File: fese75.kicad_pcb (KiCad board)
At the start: 2 copper layers, 319.1 x 133.3 mm, 209 parts, among them J1 MX-NoLED, J2 USB_C_Receptacle_USB2.0, K1 MX-NoLED, M1 MX-NoLED, P1 MX-NoLED, Q1 MX-NoLED, SW1 RotaryEncoder_Switch, T1 MX-NoLED, U1 MX-NoLED, U2 ATmega32U4-A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

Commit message: Finalize1
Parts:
- removed REF** (x3): Stabilizer_Cherry_MX_2u, Mounting_Keyboard_Stabilizer:Stabilizer_Cherry_MX_2u
- removed REF**: Stabilizer_Cherry_MX_6.25u, Mounting_Keyboard_Stabilizer:Stabilizer_Cherry_MX_6.25u
- TP1: footprint TestPoint:TestPoint_THTPad_2.0x2.0mm_Drill1.0mm -> TestPoint:TestPoint_THTPad_D1.0mm_Drill0.5mm
- TP10: value TestPoint -> CO8; moved to B.Cu
- TP11: value TestPoint -> CO9; moved to B.Cu
- TP12: value TestPoint -> CO10; moved to B.Cu
- TP13: value TestPoint -> CO11; moved to B.Cu
- TP14: value TestPoint -> CO12; moved to B.Cu
- TP15: value TestPoint -> CO13; moved to B.Cu
- TP16: value TestPoint -> CO14; moved to B.Cu
- TP17: value TestPoint -> CO15; moved to B.Cu
- TP18: value TestPoint -> RO1; moved to B.Cu
- TP19: value TestPoint -> RO2; moved to B.Cu
- TP2: footprint TestPoint:TestPoint_THTPad_D2.0mm_Drill1.0mm -> TestPoint:TestPoint_THTPad_1.0x1.0mm_Drill0.5mm
- TP20: value TestPoint -> RO3; moved to B.Cu
- TP21: value TestPoint -> RO4; moved to B.Cu
- TP22: value TestPoint -> RO5; moved to B.Cu
- TP23: value TestPoint -> RO6; moved to B.Cu
- TP3, TP4, TP5, TP6: moved to B.Cu
- TP7: value TestPoint -> CO5; moved to B.Cu
- TP8: value TestPoint -> CO6; moved to B.Cu
- TP9: value TestPoint -> CO7; moved to B.Cu
- turned TP10 to 180 degrees
- turned TP11 to 180 degrees
- turned TP12 to 180 degrees
- turned TP13 to 180 degrees
- turned TP14 to 180 degrees
- turned TP15 to 180 degrees
- turned TP16 to 180 degrees
- turned TP17 to 180 degrees
- turned TP18 to 180 degrees
- turned TP19 to 0 degrees
- turned TP20 to 0 degrees
- turned TP21 to 0 degrees
- turned TP22 to 0 degrees
- turned TP23 to 0 degrees
- turned TP3 to 180 degrees
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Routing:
- net COL3: track 316.0 -> 328.7 mm, vias 7 -> 8

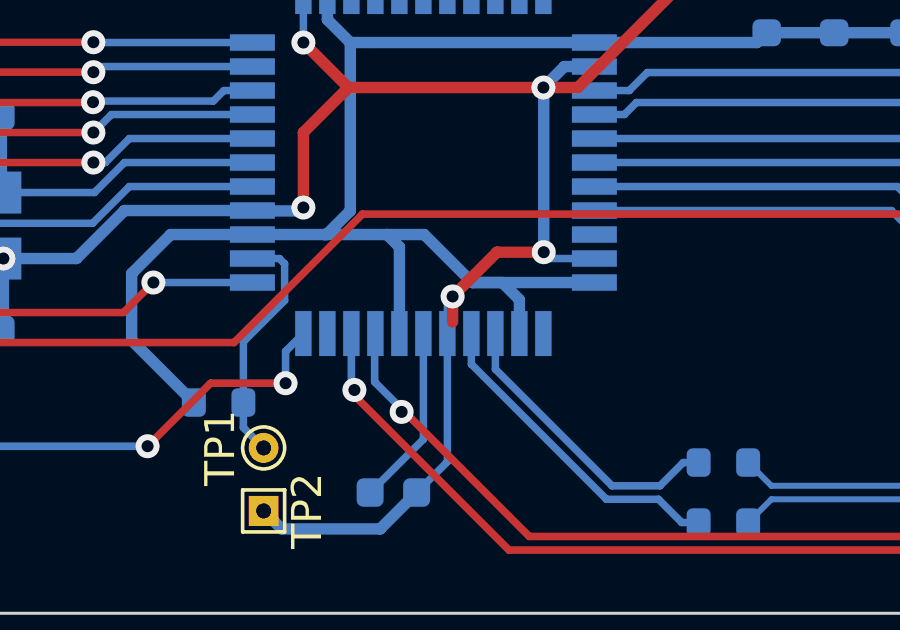
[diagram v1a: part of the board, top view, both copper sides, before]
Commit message: connect missing trace
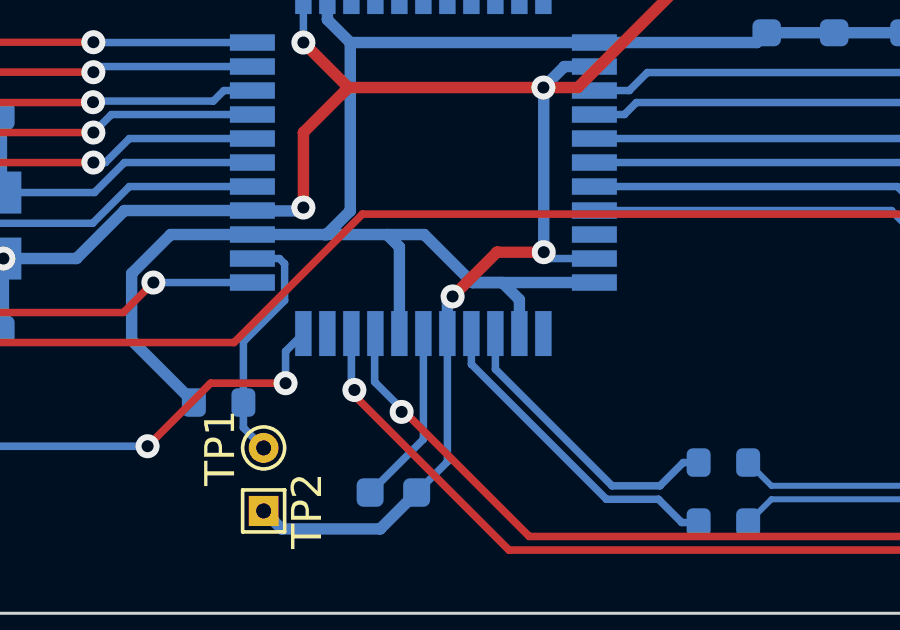
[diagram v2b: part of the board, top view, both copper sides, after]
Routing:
- net GND: track 326.8 -> 326.0 mm
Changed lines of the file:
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@@
   (segment (start 337.75 67.327222) (end 337.75 67.8875) (width 0.381) (layer "F.Cu") (net 108))
   (segment (start 331.336229 57.099979) (end 327.79375 53.5575) (width 0.381) (layer "F.Cu") (net 108))
-  (segment (start 200.898998 172.101002) (end 200.898998 171.251497) (width 0.381) (layer "F.Cu") (net 108))
   (segment (start 202.375294 169.775201) (end 203.937299 169.775201) (width 0.381) (layer "F.Cu") (net 108))
   (segment (start 184.225006 168.287497) (end 185.925003 169.987493) (width 0.381) (layer "F.Cu") (net 108))
@@
   (segment (start 198.4875 179) (end 195.2 179) (width 0.381) (layer "B.Cu") (net 108))
   (segment (start 327.42375 53.1875) (end 327.79375 53.5575) (width 0.381) (layer "B.Cu") (net 108))
-  (segment (start 200.725 171.425495) (end 200.898998 171.251497) (width 0.25) (layer "B.Cu") (net 108))
   (segment (start 188.36071 169.987493) (end 185.925003 169.987493) (width 0.381) (layer "B.Cu") (net 108))
   (segment (start 203.937299 164.299799) (end 203.937299 169.775201) (width 0.381) (layer "B.Cu") (net 108))
+  (segment (start 200.725 171.425495) (end 200.898998 171.251497) (width 0.381) (layer "B.Cu") (net 108))
   (segment (start 189.960718 168.3875) (end 188.360718 169.9875) (width 0.381) (layer "B.Cu") (net 108))
   (segment (start 319.14375 50.1775) (end 327.79375 50.1775) (width 0.381) (layer "B.Cu") (net 108))
@@
   (segment (start 185.925 172.29375) (end 185.85 172.36875) (width 0.25) (layer "B.Cu") (net 108))
   (segment (start 203.937299 169.775201) (end 204.149598 169.9875) (width 0.25) (layer "B.Cu") (net 108))
+  (segment (start 200.725 172.4875) (end 200.725 171.425495) (width 0.381) (layer "B.Cu") (net 108))
   (segment (start 210.24375 159.7875) (end 211.36875 160.9125) (width 0.381) (layer "B.Cu") (net 108))
   (segment (start 200.725 176.7625) (end 200.725 172.4875) (width 0.25) (layer "B.Cu") (net 108))
@@
   (segment (start 195.2 179) (end 194.6 178.4) (width 0.381) (layer "B.Cu") (net 108))
   (segment (start 199.7 177.7875) (end 200.725 176.7625) (width 0.25) (layer "B.Cu") (net 108))
-  (segment (start 200.725 172.4875) (end 200.725 171.425495) (width 0.25) (layer "B.Cu") (net 108))
   (segment (start 198.15 177.7875) (end 199.925 176.0125) (width 0.25) (layer "B.Cu") (net 109))
   (segment (start 199.925 176.0125) (end 199.925 172.4875) (width 0.25) (layer "B.Cu") (net 109))

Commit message: fix missing stab bug
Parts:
- added REF**: Stabilizer_Cherry_MX_2u, Mounting_Keyboard_Stabilizer:Stabilizer_Cherry_MX_2u, F.Cu at (299.6, 88.9)
- added REF**: Stabilizer_Cherry_MX_2u, Mounting_Keyboard_Stabilizer:Stabilizer_Cherry_MX_2u, F.Cu at (54.4, 146.1)
- added REF**: Stabilizer_Cherry_MX_2u, Mounting_Keyboard_Stabilizer:Stabilizer_Cherry_MX_2u, F.Cu at (297.2, 127.0)
- added REF**: Stabilizer_Cherry_MX_6.25u, Mounting_Keyboard_Stabilizer:Stabilizer_Cherry_MX_6.25u, F.Cu at (163.9, 165.1)
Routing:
- net ROW5: track 314.6 -> 316.6 mm
- net ROW2: track 451.2 -> 452.4 mm
- net COL1: track 406.9 -> 407.9 mm

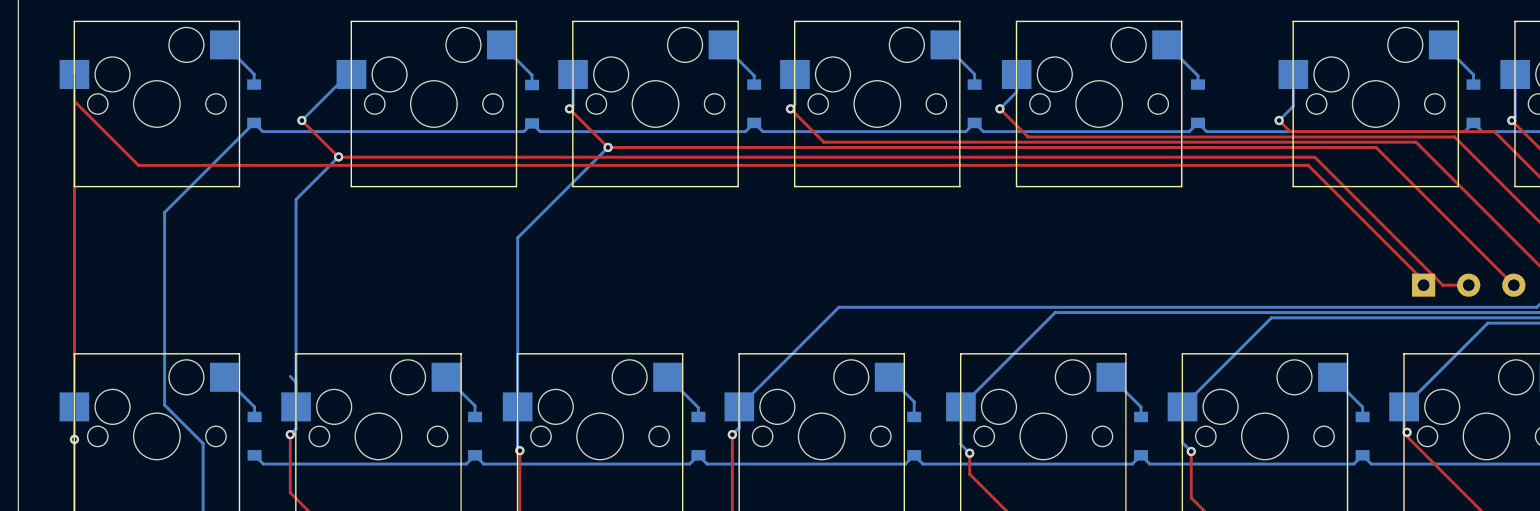
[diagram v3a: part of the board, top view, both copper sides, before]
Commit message: fix missing trace
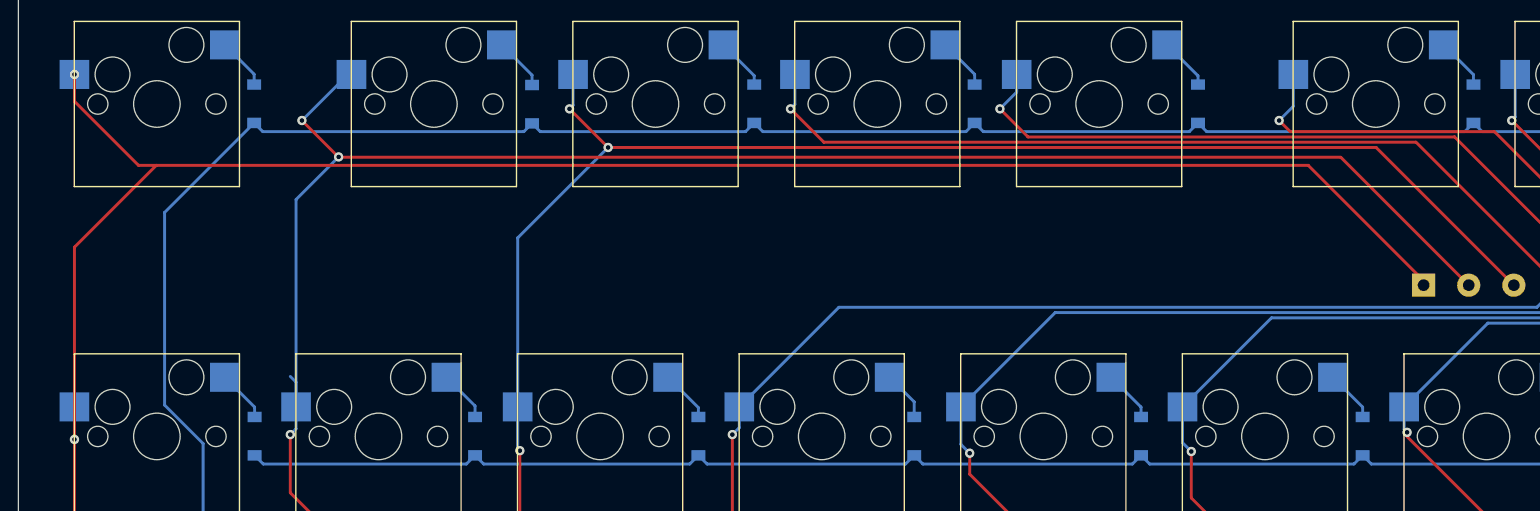
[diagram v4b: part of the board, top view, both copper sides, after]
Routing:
- net COL1: track 407.9 -> 403.2 mm, vias 6 -> 7
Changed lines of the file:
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@@
     )
     (pad_to_mask_clearance 0)
-    (grid_origin 32.93125 50.84375)
     (pcbplotparams
       (layerselection 0x00010fc_ffffffff)
@@
       (outputformat 1)
       (mirror false)
-      (drillshape 1)
+      (drillshape 0)
       (scaleselection 1)
-      (outputdirectory "")
+      (outputdirectory "C:/Users/imovi/Desktop/FESE75/Gerber/")
     )
   )
@@
   (segment (start 84.31875 124.64675) (end 84.31875 125.37125) (width 0.25) (layer "B.Cu") (net 13))
   (segment (start 76.925 146.7875) (end 70.925 152.7875) (width 0.25) (layer "F.Cu") (net 14))
-  (segment (start 58.08125 64.94375) (end 141.998562 64.94375) (width 0.254) (layer "F.Cu") (net 14))
   (segment (start 100.925 152.7875) (end 101.815625 153.678125) (width 0.25) (layer "F.Cu") (net 14))
+  (segment (start 58.08125 64.94375) (end 144.224111 64.94375) (width 0.254) (layer "F.Cu") (net 14))
   (segment (start 170.925 170.7875) (end 174.925 166.7875) (width 0.25) (layer "F.Cu") (net 14))
   (segment (start 70.925 152.7875) (end 100.925 152.7875) (width 0.25) (layer "F.Cu") (net 14))
-  (segment (start 54.925 61.7875) (end 58.08125 64.94375) (width 0.254) (layer "F.Cu") (net 14))
   (segment (start 62.925 108.7875) (end 62.925 116.7875) (width 0.25) (layer "F.Cu") (net 14))
   (segment (start 67.925 127.7875) (end 67.925 131.7875) (width 0.25) (layer "F.Cu") (net 14))
@@
   (segment (start 53.925 93.7875) (end 62.925 102.7875) (width 0.25) (layer "F.Cu") (net 14))
   (segment (start 101.815625 153.678125) (end 125.009375 153.678125) (width 0.25) (layer "F.Cu") (net 14))
-  (segment (start 152.998562 75.94375) (end 155.224111 75.94375) (width 0.254) (layer "F.Cu") (net 14))
-  (segment (start 141.998562 64.94375) (end 152.998562 75.94375) (width 0.254) (layer "F.Cu") (net 14))
+  (segment (start 54.925 61.7875) (end 58.08125 64.94375) (width 0.254) (layer "F.Cu") (net 14))
   (segment (start 67.925 131.7875) (end 76.925 140.7875) (width 0.25) (layer "F.Cu") (net 14))
   (segment (start 125.009375 153.678125) (end 142.11875 170.7875) (width 0.25) (layer "F.Cu") (net 14))
+  (segment (start 144.224111 64.94375) (end 155.224111 75.94375) (width 0.254) (layer "F.Cu") (net 14))
   (segment (start 142.11875 170.7875) (end 170.925 170.7875) (width 0.25) (layer "F.Cu") (net 14))
   (via (at 67.925 121.7875) (size 0.8) (drill 0.4) (layers "F.Cu" "B.Cu") (net 14))
@@
   (segment (start 276.89825 161.63575) (end 279.25625 163.99375) (width 0.25) (layer "B.Cu") (net 26))
   (segment (start 276.89825 160.06375) (end 276.89825 161.63575) (width 0.25) (layer "B.Cu") (net 26))
+  (segment (start 35.37125 89.20375) (end 35.37125 72.67875) (width 0.254) (layer "F.Cu") (net 27))
   (segment (start 40.13375 122.1225) (end 40.13375 139.54625) (width 0.254) (layer "F.Cu") (net 27))
+  (segment (start 35.37125 72.67875) (end 42.40625 65.64375) (width 0.254) (layer "F.Cu") (net 27))
   (segment (start 60.775 151.7875) (end 63.966771 154.979271) (width 0.254) (layer "F.Cu") (net 27))
+  (segment (start 42.40625 65.64375) (end 141.43125 65.64375) (width 0.254) (layer "F.Cu") (net 27))
   (segment (start 40.13375 105.64125) (end 40.13375 107.54625) (width 0.25) (layer "F.Cu") (net 27))
   (segment (start 69.695729 154.979271) (end 70.8875 153.7875) (width 0.254) (layer "F.Cu") (net 27))
@@
   (segment (start 43.88125 143.29375) (end 48.925 148.3375) (width 0.254) (layer "F.Cu") (net 27))
   (segment (start 38.23125 160.34375) (end 39.781783 160.34375) (width 0.254) (layer "F.Cu") (net 27))
-  (segment (start 35.37125 57.82875) (end 35.37125 58.08375) (width 0.25) (layer "F.Cu") (net 27))
   (segment (start 35.37125 89.20375) (end 35.37125 100.69125) (width 0.25) (layer "F.Cu") (net 27))
   (segment (start 40.13375 139.54625) (end 43.88125 143.29375) (width 0.254) (layer "F.Cu") (net 27))
@@
   (segment (start 48.925 151.200533) (end 48.925 150.7875) (width 0.254) (layer "F.Cu") (net 27))
   (segment (start 106.565625 160.428125) (end 120.565625 160.428125) (width 0.25) (layer "F.Cu") (net 27))
-  (segment (start 35.37125 58.08375) (end 35.37125 60.133669) (width 0.254) (layer "F.Cu") (net 27))
+  (segment (start 40.881331 65.64375) (end 42.40625 65.64375) (width 0.254) (layer "F.Cu") (net 27))
   (segment (start 49.925 151.7875) (end 60.775 151.7875) (width 0.25) (layer "F.Cu") (net 27))
   (segment (start 35.37125 100.69125) (end 40.13375 105.45375) (width 0.254) (layer "F.Cu") (net 27))
   (segment (start 141.43125 65.64375) (end 151.34554 75.55804) (width 0.254) (layer "F.Cu") (net 27))
   (segment (start 131.925 171.7875) (end 189.925 171.7875) (width 0.25) (layer "F.Cu") (net 27))
-  (segment (start 40.881331 65.64375) (end 141.43125 65.64375) (width 0.254) (layer "F.Cu") (net 27))
+  (segment (start 35.37125 60.133669) (end 35.37125 57.82875) (width 0.254) (layer "F.Cu") (net 27))
   (segment (start 39.781783 160.34375) (end 48.925 151.200533) (width 0.254) (layer "F.Cu") (net 27))
-  (segment (start 35.37125 58.08375) (end 35.37125 86.40375) (width 0.25) (layer "F.Cu") (net 27))
-  (segment (start 35.37125 86.40375) (end 35.37125 89.20375) (width 0.25) (layer "F.Cu") (net 27))
   (segment (start 63.966771 154.979271) (end 69.695729 154.979271) (width 0.254) (layer "F.Cu") (net 27))
   (segment (start 151.34554 75.55804) (end 151.34554 75.94375) (width 0.254) (layer "F.Cu") (net 27))
@@
   (via (at 190.925 170.7875) (size 0.8) (drill 0.4) (layers "F.Cu" "B.Cu") (net 27))
   (via (at 38.23125 160.34375) (size 0.8) (drill 0.4) (layers "F.Cu" "B.Cu") (net 27))
+  (via (at 35.37125 57.82875) (size 0.8) (drill 0.4) (layers "F.Cu" "B.Cu") (net 27))
   (via (at 40.13375 107.54625) (size 0.8) (drill 0.4) (layers "F.Cu" "B.Cu") (net 27))
   (via (at 43.88125 143.29375) (size 0.8) (drill 0.4) (layers "F.Cu" "B.Cu") (net 27))
